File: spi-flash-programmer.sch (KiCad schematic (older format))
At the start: 49 parts, among them Q1 BSS138, Q2 BSS138, Q4 BSS138, Q5 BSS138, SW1 SW_SPDT, SW2 SW_SPDT, U1 TXB0104D, U3 AP2127K-ADJ, U4 MX25L25735, U5 AT25SF081-SSHD-X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

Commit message: Added jumper to work with Rock64 board which lacks CS1.
Signed-off-by: Aaron Williams <aaron.w2@gmail.com>
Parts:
- added J1: Conn_01x03, Pin_Headers:Pin_Header_Straight_1x03_Pitch2.54mm, symbol Connector_Generic:Conn_01x03
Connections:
- wire segments 86 -> 90
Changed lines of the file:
@@
 Title "Raspberry PI SPI flash hat"
 Date "2019-01-26"
-Rev "2.0"
+Rev "2.1.0"
 Comp "Copyright (C) 2019 Aaron Williams"
 Comment1 ""
@@
 	3900 6450 3900 6700
 Connection ~ 3900 6450
-Text GLabel 1600 3850 0    50   Input ~ 0
+Text GLabel 1200 4700 0    50   Input ~ 0
 R_FL_CS1
-Text Label 1600 3850 0    50   ~ 0
+Text Label 1250 4700 0    50   ~ 0
 R_FL_CS1
 $Comp
@@
 FL_CS1
 Wire Wire Line
-	1950 4000 1600 4000
-Text Label 1600 4000 0    50   ~ 0
+	1950 4000 1800 4000
+Text Label 1800 4000 0    50   ~ 0
 OE
 $Comp
@@
 Text Notes 6450 1750 0    50   ~ 0
 White power LED
-Wire Wire Line
-	1600 3850 1950 3850
+$Comp
+L Connector_Generic:Conn_01x03 J1
+U 1 1 5C54EE1D
+P 1900 4600
+F 0 "J1" H 1980 4642 50  0000 L CNN
+F 1 "Conn_01x03" H 1980 4551 50  0000 L CNN
+F 2 "Pin_Headers:Pin_Header_Straight_1x03_Pitch2.54mm" H 1900 4600 50  0001 C CNN
+F 3 "~" H 1900 4600 50  0001 C CNN
+	1    1900 4600
+	1    0    0    -1
+$EndComp
+Wire Wire Line
+	1200 4700 1700 4700
+Wire Wire Line
+	1700 4500 1200 4500
+Text Label 1250 4500 0    50   ~ 0
+R_FL_CS0
+Wire Wire Line
+	1700 4600 1650 4600
+Wire Wire Line
+	1650 4600 1650 3850
+Wire Wire Line
+	1650 3850 1950 3850
 $EndSCHEMATC

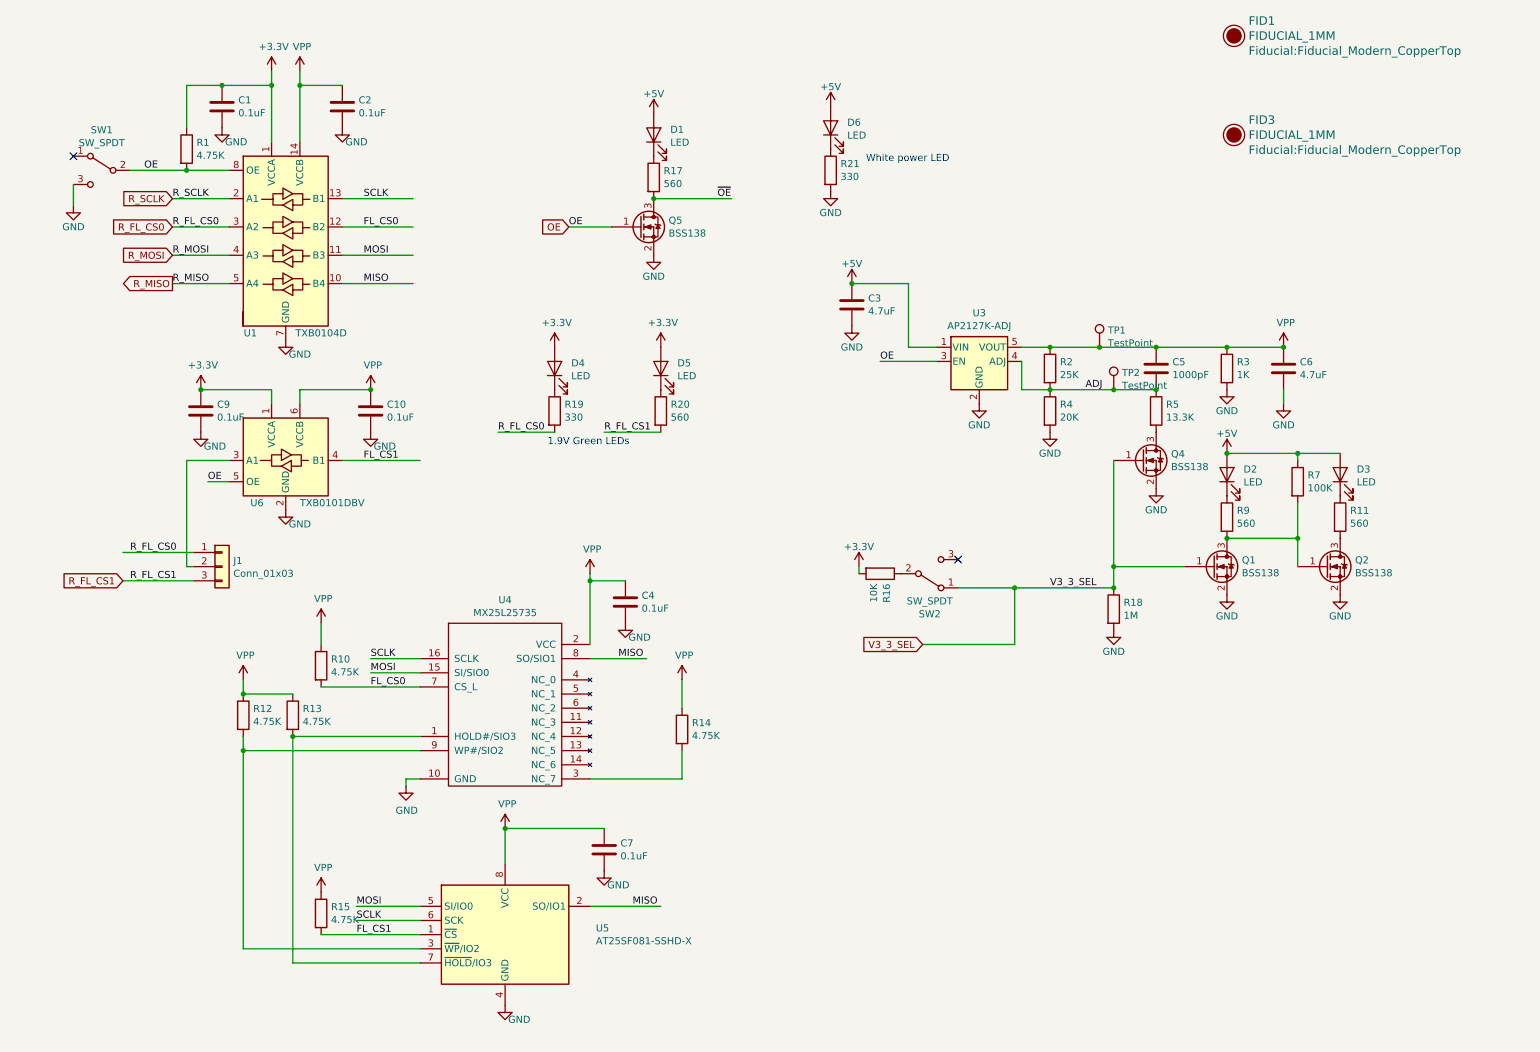
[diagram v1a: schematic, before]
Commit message: Fixes a number of issues
This fixes a number of issues with the previous design.

1. The OE GPIO pin was not hooked up.
2. The level shifter has been changed to a 5 channel unidirectional
   level shifter.
3. LEDs were moved down near the base.
4. The switches were fixed based on measuring the contacts with different
   switch positions (not in the data sheet).
5. Added support for some non-Raspberry PI boards.
6. Changed resistors in power supply based on what is readily available.

Signed-off-by: Aaron Williams <aaron.w2@gmail.com>
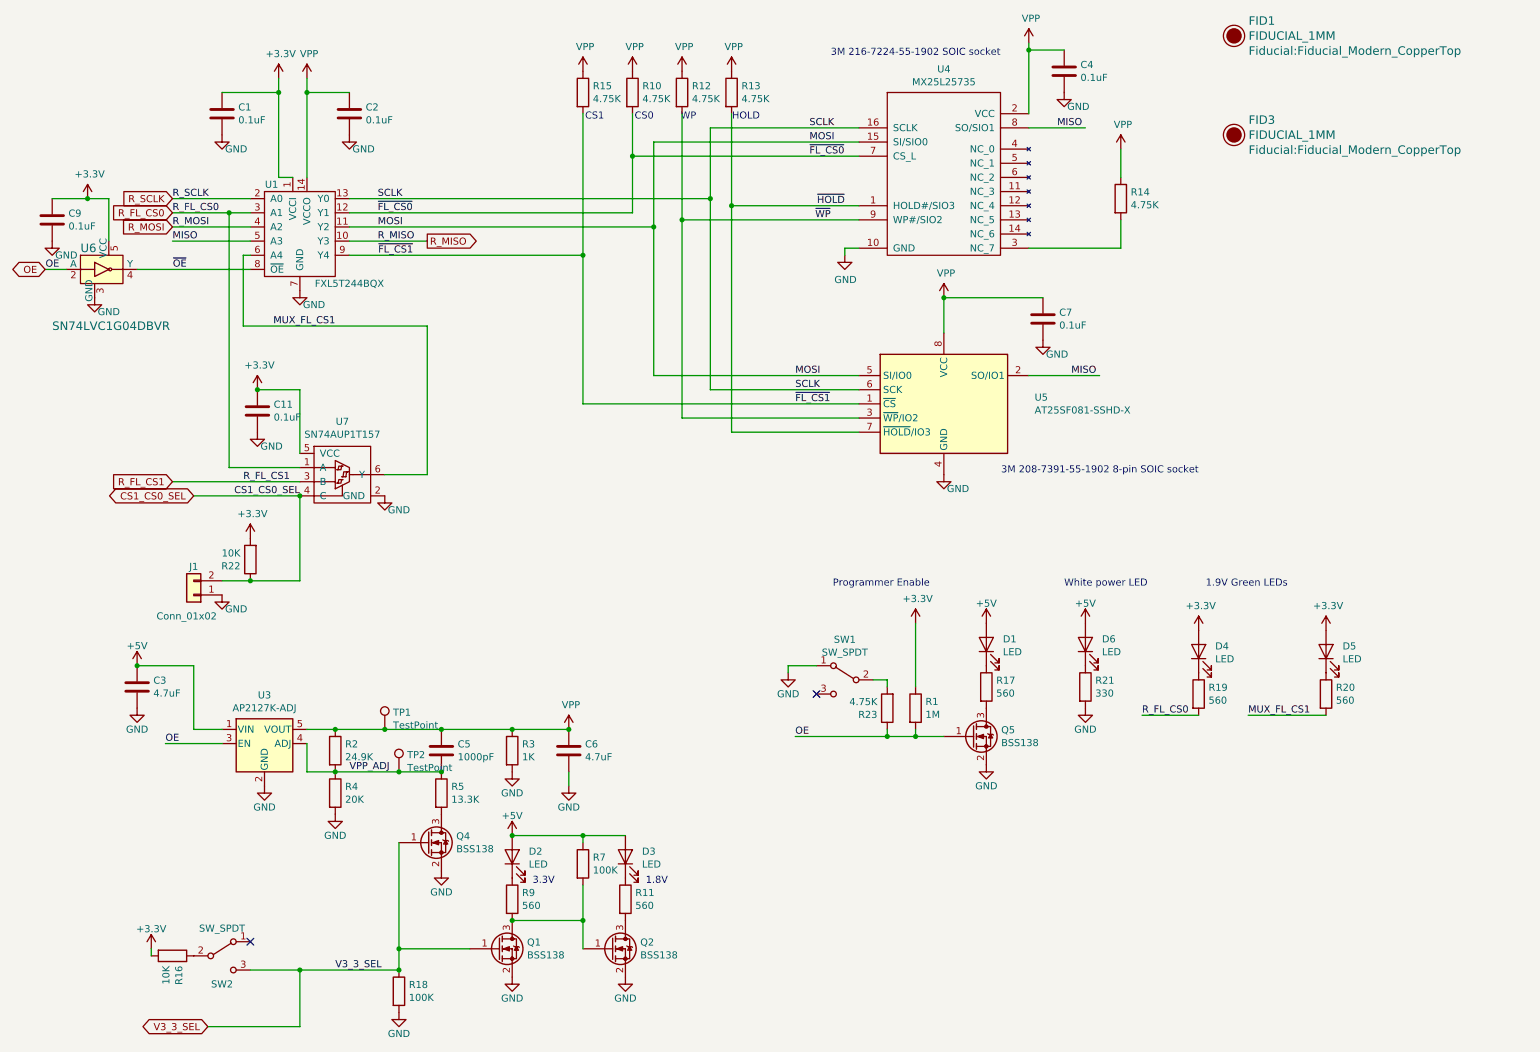
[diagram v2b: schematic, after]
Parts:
- removed C10: 0.1uF, Capacitor_SMD:C_0603_1608Metric, symbol raspberry-spi-flash2-rescue:C-device-raspberry-spi-flash-rescue
- removed J1: Conn_01x03, Pin_Headers:Pin_Header_Straight_1x03_Pitch2.54mm, symbol Connector_Generic:Conn_01x03
- removed U1: TXB0104D, Package_SO:SOIC-14_3.9x8.7mm_P1.27mm, symbol Logic_LevelTranslator:TXB0104D
- removed U6: TXB0101DBV, Package_TO_SOT_SMD:TSOT-23-6, symbol Aaron:TXB0101DBV
- added C11: 0.1uF, Capacitor_SMD:C_0603_1608Metric, symbol raspberry-spi-flash2-rescue:C-device-raspberry-spi-flash-rescue
- added J1: Conn_01x02, Connector_PinHeader_2.54mm:PinHeader_1x02_P2.54mm_Vertical, symbol Connector_Generic:Conn_01x02
- added R22: 10K, Resistor_SMD:R_0603_1608Metric, symbol raspberry-spi-flash2-rescue:R-device-raspberry-spi-flash-rescue
- added R23: 4.75K, Resistor_SMD:R_0603_1608Metric, symbol Device:R
- added U1: FXL5T244BQX, Aaron:DQFN-14-1EP_2.5x3mm_EP2.2x1.7mm_Thermal, symbol Aaron:FXL5T244BQX
- added U6: SN74LVC1G04DBVR, digikey-footprints:SOT-753, symbol dk_Logic-Gates-and-Inverters:SN74LVC1G04DBVR
- added U7: SN74AUP1T157, Package_TO_SOT_SMD:SOT-23-6, symbol Aaron:SN74AUP1T157
- R1: value 4.75K -> 1M
- R18: value 1M -> 100K
- R19: value 330 -> 560
- R2: value 25K -> 24.9K; MFR (none) -> Yageo; MPN (none) -> RT0603DRE0724K3L; SPN (none) -> 311-2496-1-ND; SPR (none) -> Digikey; SPURL (none) -> https://www.digikey.com/product-detail/en/yageo/RT0603DRE07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
- R4: MFR (none) -> Yageo; MPN (none) -> RT0603FRE0720KL; SPN (none) -> YAG5727CT-ND; SPR (none) -> Digikey; SPURL (none) -> https://www.digikey.com/product-detail/en/yageo/RT0603FRE07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
- R5: MFR (none) -> Vishay Dale; MPN (none) -> CRCW060313K3FKEA; SPN (none) -> 541-13.3KHCT-ND; SPR (none) -> Digikey; SPURL (none) -> https://www.digikey.com/product-detail/en/vishay-dale/CRCW0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
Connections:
- net labels added: CS1_CS0_SEL, MUX_FL_CS1, VPP_ADJ, ~FL_CS0, ~FL_CS1, ~HOLD, ~WP
- net labels removed: ADJ, FL_CS0, FL_CS1
- wire segments 90 -> 110
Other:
- note added: "1.8V"
- note added: "3.3V"
- note added: "3M 208-7391-55-1902 8-pin SOIC socket"
- note added: "3M 216-7224-55-1902 SOIC socket"
- note added: "CS0"
- note added: "CS1"
- note added: "HOLD"
- note added: "Programmer Enable"
- note added: "WP"
- moved on the sheet: C1, C2, C3, C4, C5, C6, C7, D1, D2, D3, D4, D5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
